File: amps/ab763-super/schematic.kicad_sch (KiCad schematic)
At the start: 112 parts, among them T1 125P5D · 360-0-360V, T2 125C1A, T3 125A9A, T4 125A20B

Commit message: Fix: deterministic schematic ids and wires split at every join
- _u() is uuid5 over (amp id, emission order), so a regeneration of an
  unchanged script is byte-identical and a drift gate becomes possible
- write() splits wire segments at symbol pins, wire ends and junction dots,
  so the file connects exactly what the drawing shows under KiCad's
  endpoint-only semantics (270 pins were on a wire's interior; net
  partitions unchanged on all 38 sheets)
- all sheets regenerated; aa864-bassman title block was stale (draft) and
  now matches meta.yaml (verified)

Co-Authored-By: Claude Fable 5.1 <noreply@anthropic.com>
Claude-Session: https://claude.ai/code/session_01KBMfdh37HmCL2iWcBiL5J1
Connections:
- net at RBIAS.1: now also DBIAS.2 (K)
- net at T3.1 (PRI_A): now also V7.1 (P)

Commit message: Fix: schematic wiring on ab763-twin, ab763, ab763-super
- long-tailed pair: the tail lead came off section B's PLATE pin; redrawn
  from its cathode on a joined-cathode lane under the bottle (all three)
- ab763-twin: V9/V10 plate run passed through V10's envelope and grounded
  cathode pin (one plate on ground, one floating); screen stubs 2 mm short
  of RSC1-4; V5B had no plate lead; driver grid bus through RGRD and CPIB
  riser through RFB1 (feedback node grounded); seven leads 4 mm short of
  their labels; VRBAL wiper carries -52 V per net_map
- ab763: same tail and RGRD faults; three pot ground flags 3.81 mm low;
  RNF2 had a wire ruled through its body
- ab763-super: V8 plate lead drawn from below its cathode; both reservoir
  bleeders shorted the supply to ground; RLV2 shorted by the stack output
  column; tremolo intensity feed ran through CTO1/VRSPD/RTO1 to ground;
  BP1 tap landed inside the choke body
- all three pass connectivity and verify_schematic_nets; no waivers

Co-Authored-By: Claude Fable 5.1 <noreply@anthropic.com>
Claude-Session: https://claude.ai/code/session_01KBMfdh37HmCL2iWcBiL5J1
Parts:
- removed C1: .1u 400V, symbol cx:C
- removed C11: 20u 525V, symbol cx:C
- removed CCR1: .003u, symbol cx:C
- removed CCV2: .02u, symbol cx:C
- removed CKTO1: 25u, symbol cx:C
- removed RBIAS: 470, symbol cx:R
- removed RKV2: 820, symbol cx:R
- removed RLR1: 100k, symbol cx:R
- removed RS2: 470 1W, symbol cx:R
- removed RTO2: 220k, symbol cx:R
- removed RTOG: 1M, symbol cx:R
- removed V6A: 12AT7, symbol cx:TRIODE
- removed V8: 6L6GC, symbol cx:PENTODE
- added C12: 20u 525V, symbol cx:C
- added C2: .1u 400V, symbol cx:C
- added CKV2: 25u, symbol cx:C
- added CPIB: .1u 200V, symbol cx:C
- added OPTO: neon + photocell, symbol cx:OPTO
- added RBL2: 220k 1W, symbol cx:R
- added RGR1: 220k, symbol cx:R
- added RST1: 1.5k, symbol cx:R
- added RTO1: 100k, symbol cx:R
- added V2B, V3A, V3B, V5: 12AX7, symbol cx:TRIODE
- C1: renamed from CPIB; value .1u 200V -> .1u 400V
- C11: renamed from RBL2; value 220k 1W -> 20u 525V; symbol cx:R -> cx:C
- CCD1: renamed from RKD1; value 820 -> .001u; symbol cx:R -> cx:C
- CCR1: renamed from RKR1; value 820 -> .003u; symbol cx:R -> cx:C
- CCV2: renamed from CKV2; value 25u -> .02u
- CKTO1: renamed from V5; value 12AX7 -> 25u; symbol cx:TRIODE -> cx:C
- CTO2: renamed from RTO1; value 100k -> .01u; symbol cx:R -> cx:C
- RBIAS: renamed from C12; value 20u 525V -> 470; symbol cx:C -> cx:R
- RKD1: renamed from V3A; value 12AX7 -> 820; symbol cx:TRIODE -> cx:R
- RKR1: renamed from V3B; value 12AX7 -> 820; symbol cx:TRIODE -> cx:R
- RKV2: renamed from RLV2; value 100k -> 820
- RLR1: renamed from RGR1; value 220k -> 100k
- RLV2: renamed from V2B; value 12AX7 -> 100k; symbol cx:TRIODE -> cx:R
- RS2: renamed from V7; value 6L6GC -> 470 1W; symbol cx:PENTODE -> cx:R
- RTO2: renamed from CCD1; value .001u -> 220k; symbol cx:C -> cx:R
- RTOG: renamed from CTO2; value .01u -> 1M; symbol cx:C -> cx:R
- V6A: renamed from OPTO; value neon + photocell -> 12AT7; symbol cx:OPTO -> cx:TRIODE
- V7: renamed from C2; value .1u 400V -> 6L6GC; symbol cx:C -> cx:PENTODE
- V8: renamed from RST1; value 1.5k -> 6L6GC; symbol cx:R -> cx:PENTODE
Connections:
- net BC: now also C12.1; no longer RBIAS.1
- net BD: now also RLR1.1; no longer CRS.2, RKV2.1, RKV2.2, RLV2.2 (G), SWBV.2, VRVV.2 (W)
- net BIAS TAP: now also DBIAS.1 (A)
- net BP1: now also C11.1, RD1.1, RS2.2, RTO2.1, T2.2
- net GND: now also RKD1.2, RKR1.2, RKV2.2, V7.4 (K), V8.4 (K), C12.2, CKV2.2, OPTO.2 (L2), OPTO.4 (P2), RBL2.2, RTO1.2, V5.2 (G); no longer C10.1, CCD1.2, CCR1.2, CCV2.2, CKTO1.1 (P), CTO1.1, CTO1.2, CTO2.2, RBIAS.2, RGRD.1, RINT.1, RS2.4 (K), T2.1, V4A.2 (G), V4B.2 (G), V6A.2 (L2), V6A.4 (P2), V9A.2 (K), V9B.2 (K), VRSPD.3
- net MIXG: now also CCV2.2, OPTO.3 (P1); no longer V6A.3 (P1)
- net NORM 1: now also R1n.1
- net NORM 2: now also R2n.1
- net PIG: now also CCD1.2, CPIA.1; no longer RTO2.2
- net RVSEND: now also RGRD.1, V4A.2 (G), V4B.2 (G)
- net SPKR: now also RNFB.1
- net TANK RET: now also RGR1.1
- net VIB 1: now also R1v.1
- net VIB 2: now also R2v.1
- net at DBIAS.2 (K): now also RBIAS.1
- net at CBIAS.1, VRBIAS.1: now also RBIAS.2, VRBIAS.2 (W)
- net at RKTO1.1: now also CKTO1.1, V5.3 (K); no longer CKTO1.3 (K)
- net at VRSPD.1: now also CTO1.2, CTO2.2, VRSPD.2 (W)
- net at RKR1.1: now also CKR1.1, V3B.3 (K)
- net at RLR1.2: now also CCR1.1, V3B.1 (P); no longer RKR1.2 (G)
- net at RGPB.2, V6B.2 (G): now also CPIB.2; no longer C1.2
- net at CPIA.2, RGPA.1: now also V6A.2 (G)
- net at C1.1: now also RLPA.2, V6A.1 (P); no longer RNFB.2
- net at RLPB.2, V6B.1 (P): now also C2.1; no longer RTAIL.2, V7.1
- net at VRREV.1: now also CCR1.2
- net at RS1.1: now also V7.3 (G2)
- net at CBD1.1, RGD1.1, RMR2.1: now also V3A.2 (G); no longer RKD1.2 (G)
- net at CCV2.1: now also CRS.2, RLV2.2, V2B.1 (P); no longer RLV2.3 (K)
- net at CBD1.2, RLD1.2: now also CCD1.1, V3A.1 (P); no longer RKD1.1 (P), RTO2.1
- net at RS2.1: now also V8.3 (G2); no longer T3.1 (PRI_A)
- net at T3.3 (PRI_B): now also V8.1 (P)
- net at RGL1.2: now also C1.2, RST1.1; no longer V8.1
- net at VRINT.1: now also CTO1.1, RTO2.2, VRINT.2 (W), V5.1 (P)
- net at VRINT.3: now also RINT.1
- net at RINT.2: now also OPTO.1 (L1); no longer V6A.1 (L1)
- net at RST2.2: now also V8.2 (G1)
- net at RGL2.1, RST2.1: now also C2.2; no longer V7.2
- net at RBL1.1: now also C10.1, T2.1, V9A.2 (K), V9B.2 (K), RBL2.1
- net at V6B.3 (K): now also RTAIL.2, V6A.3 (K)
- new net: CKD1.1, RKD1.1, V3A.3 (K)
- new net: RST1.2, V7.2 (G1)
- new net: RGR1.2, V3B.2 (G)
- new net: RTO1.1, VRSPD.3
- new net: SWBV.2, V2B.2 (G), VRVV.2 (W)
- new net: CKV2.1, RKV2.1, V2B.3 (K)
- new net: CPIB.1, RNFB.2
- new net: T3.1 (PRI_A), V7.1 (P)
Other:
- moved on the sheet: C1, CCV2, RGRD, RKV2, RLR1

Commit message: Fix: AB763 Super and 6G4 corrections read back from the factory sheets
AB763 Super (closes #15, closes #16)

The model omitted the Normal channel's second triode entirely and gave the
Vibrato second stage, mix driver and reverb recovery a cathode resistor each.
The C-FD schematic's boxed [A] and [E] are inter-stage connections: [A] ties
the Normal and Vibrato second stages to ONE 820 / 25u network, [E] ties the mix
driver and reverb recovery to another. Because our model omitted one triode's
current, this page claimed the printed chart was internally impossible at three
cathode nodes. It is not. With XV1B added and the shared nodes joined:

  KA   chart 2.1 V   was 1.5 V (-30.0%)   now 2.2 V (+3.6%)
  KE   chart 2.0 V   was 1.5 V (-27.0%)   now 2.2 V (+8.8%)
  PV2  chart 270 V   was 231 V (-14.4%)   now 277 V (+2.6%)

All 20 gated nodes now pass; the accusation is retracted in notes.md and the
retraction is recorded in meta.yaml as audit trail. This is the fourth time the
corpus has accused a factory sheet and been the one at fault.

The Middle control is 10 kOhm-A, not the 250 kOhm published -- 25x, so the
tone-stack curve was wrong, not just the label. Corrected everywhere including
the lab preset; the blackface mid-scoop returns at 15.6 dB / 419 Hz.

With the Middle pot confirmed, topology.tone_stack moves tb -> fmv: this
chassis carries a fixed bleed on one channel and a real Middle pot on the
other, and filing it as treble/bass contradicted its own parts list. The field
names the Vibrato channel and notes.md documents the mixed case.

6G4

Same presence idiom as the 6G5, read off the A-FJ sheet: a 1500 foot resistor
to ground with the 5K-L pot in series with a .1 cap paralleling it. The cap was
missing from the corpus; added as CPRES, 0.1uF, the 200 V read off the layout
page's own .1-200 lettering rather than defaulted from the notice's 400 V.

RNFB is 10 kOhm, not 56 -- traced end to end onto the OT secondary hot. RD1 is
4700 1W, not 10k: the netlist called t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
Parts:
- removed C1: .1u 400V, symbol cx:C
- removed CBV: .1u, symbol cx:C
- removed CCD1: .001u, symbol cx:C
- removed CKR1, CKV2: 25u, symbol cx:C
- removed CTO2: .01u, symbol cx:C
- removed R1v: 68k, symbol cx:R
- removed RBL1: 220k 1W, symbol cx:R
- removed RGPA, RGRD: 1M, symbol cx:R
- removed RGR1, RMR2: 220k, symbol cx:R
- removed RKD1, RKR1: 820, symbol cx:R
- removed RMR: 470k, symbol cx:R
- removed V2A: 12AX7, symbol cx:TRIODE
- removed VRVV: 1M-A vol, symbol cx:POT
- added C11: 20u 525V, symbol cx:C
- added CCN2: .047u, symbol cx:C
- added CCR1: .003u, symbol cx:C
- added CCV2: .02u, symbol cx:C
- added CKA, CKE: 25u, symbol cx:C
- added CRS: 500p, symbol cx:C
- added CTV: 250p, symbol cx:C
- added OPTO: neon + photocell, symbol cx:OPTO
- added RGL2: 220k 5%, symbol cx:R
- added RKE, RNFB: 820, symbol cx:R
- added RLN2, RLR1, RLV1: 100k, symbol cx:R
- added RTO2: 220k, symbol cx:R
- added RTOG: 1M, symbol cx:R
- added V1B: 12AX7, symbol cx:TRIODE
- C1: renamed from RGL2; value 220k 5% -> .1u 400V; symbol cx:R -> cx:C
- CBV: renamed from VRMV; value 250k-A mid -> .1u; symbol cx:POT -> cx:C
- CCD1: renamed from CTO1; value .01u -> .001u
- CTO1: renamed from RTOG; value 1M -> .01u; symbol cx:R -> cx:C
- CTO2: renamed from OPTO; value neon + photocell -> .01u; symbol cx:OPTO -> cx:C
- R1v: renamed from RLV1; value 100k -> 68k
- RBL1: renamed from C11; value 20u 525V -> 220k 1W; symbol cx:C -> cx:R
- RGPA: renamed from RNFB; value 820 -> 1M
- RGR1: renamed from CCR1; value .003u -> 220k; symbol cx:C -> cx:R
- RGRD: renamed from T4; value 125A20B -> 1M; symbol cx:OT_SE -> cx:R
- RKA: renamed from CRS; value 500p -> 820; symbol cx:C -> cx:R
- RMR: renamed from V3A; value 12AX7 -> 470k; symbol cx:TRIODE -> cx:R
- RMR2: renamed from CKD1; value 25u -> 220k; symbol cx:C -> cx:R
- SWBV: renamed from RKV2; value 820 -> Bright; symbol cx:R -> cx:SWITCH
- T4: renamed from RLR1; value 100k -> 125A20B; symbol cx:R -> cx:OT_SE
- V2A: renamed from CTV; value 250p -> 12AX7; symbol cx:C -> cx:TRIODE
- V2B: renamed from CCV2; value .02u -> 12AX7; symbol cx:C -> cx:TRIODE
- V3A: renamed from RTO2; value 220k -> 12AX7; symbol cx:R -> cx:TRIODE
- VRMV: renamed from SWBV; value Bright -> 10k-A mid; symbol cx:SWITCH -> cx:POT
- VRVV: renamed from V2B; value 12AX7 -> 1M-A vol; symbol cx:TRIODE -> cx:POT
- renumbered V1 to V1A
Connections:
- net -52V: now also RGL2.2; no longer C1.2
- net BD: now also RLN2.1, RLR1.1, RLV1.1; no longer R1v.1, T4.1
- net BP1: now also C11.1, RTO2.1; no longer RBL1.1, V3A.1
- net GND: now also CTO2.1, RGRD.2, RKA.2, T4.4 (SEC_C), VRMV.3, VRVV.3, C11.2, CKA.2, CKE.2, OPTO.2 (L2), OPTO.4 (P2), RKE.2, RTOG.1, RTOG.2; no longer CBV.3, CTO1.1, CTO1.2, CTO2.2 (L2), CTO2.4 (P2), RGRD.4 (SEC_C), SWBV.2
- net MIXG: now also RMR.2, CCV2.2, OPTO.3 (P1); no longer CTO2.3 (P1), V2B.2
- net PIG: now also CCD1.2
- net REVERB TANK: now also T4.3 (SEC_H); no longer RGRD.3 (SEC_H)
- net RVSEND: now also RGRD.1, CRS.1; no longer RKA.1
- net SPKR: now also RNFB.1; no longer RGPA.1
- net TANK RET: now also RGR1.1
- net VIB 1: now also R1v.1
- net at CBV2.1, RSV.2: now also CBV.1
- net at RINT.2: now also OPTO.1 (L1); no longer CTO2.1 (L1)
- net at RGR1.2: now also V3B.2 (G); no longer VRREV.1
- net at CBD1.2, RLD1.2: now also CCD1.1, V3A.1 (P); no longer RMR.1 (P)
- net at CBD1.1, RGD1.1: now also RMR2.1, V3A.2 (G); no longer RMR.2 (G)
- net at RGPB.1, RT2.1, RTAIL.1: now also RGPA.2
- net at RGL1.2, RST1.1: now also C1.2
- net at VRREV.2 (W): now also RMR.1
- net at RSV.1, V2A.1 (P): now also CTV.1, RLV1.2; no longer R1v.2
- net at VRSPD.1, VRSPD.2 (W): now also CTO1.2, CTO2.2; no longer CCD1.2
- net KE: now reaches V3B.3 (K)
- net KE: now also V3A.3 (K), CKE.1, RKE.1
- net at V5.1 (P), VRINT.1, VRINT.2 (W): now also CTO1.1, RTO2.2; no longer CCD1.1, V3A.2
- net at C2.2, RST2.1: now also RGL2.1; no longer C1.1
- net at RLPA.2, V6A.1 (P): now also C1.1
- net at SWBN.2, VRVN.2 (W): now also V1B.2 (G); no longer RMD1.1
- net at CKV1.1, RKV1.1: now also V2A.3 (K)
- net at C10.1, RBL2.1, T2.1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: now also RBL1.1
- net at V2A.2 (G): now also R1v.2, R2v.2, RGV1.1; no longer VRTV.1
- net at CBRV.1, VRTV.2 (W): now also VRVV.1
- net at CPIA.2, V6A.2 (G): now also RGPA.1
- net at RLV2.2, V2B.1 (P): now also CCV2.1, CRS.2; no longer RKA.2, VRVV.1 (P)
- net at VRMV.1: now also VRBV.3, VRMV.2 (W); no longer CBRV.2
- net at VRVV.2 (W): now also SWBV.2, V2B.2 (G); no longer VRMV.2
- net at SWBV.1: now also CBRV.2; no longer VRVV.3 (K)
- net at CPIB.1: now also RNFB.2; no longer RGPA.2
- new net: CTV.2, VRTV.1
- new net: CCN2.2, RMD1.1
- new net: CCN2.1, RLN2.2, V1B.1 (P)
- new net: CCR1.1, RLR1.2, V3B.1 (P)
- new net: CCR1.2, VRREV.1
- new net KA: CKA.1, RKA.1, V1B.3 (K), V2B.3 (K)
- now unconnected: CBV.2 (W), T4.2
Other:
- note added: "1"
- note added: "2"
- note added: "3"
- note added: "4"
- note added: "5"
- note added: "6"
- note added: "7"
- note added: "8"
- moved on the sheet: CCD1, R1v, RGPA, VRMV

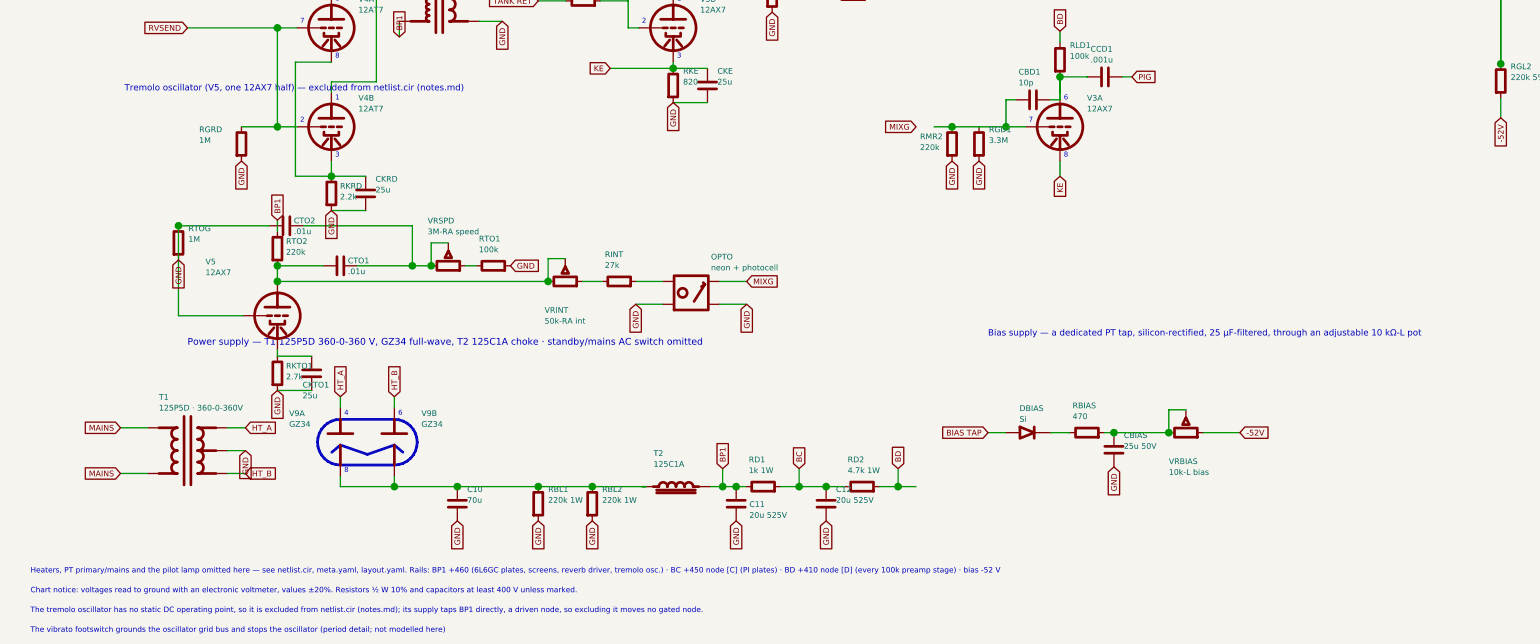
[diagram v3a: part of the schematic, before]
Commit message: Fix: schematic sheet notes no longer name repository files
Thirty-seven committed sheets rendered footnotes and section notes such as
"Heaters and PT primary omitted — see netlist.cir and meta.yaml" or
"excluded from netlist.cir (notes.md)" to visitors through KiCanvas. The
prose sweeps never counted sheets. Rewritten in the site's own words — the
netlist, the sources list, the circuit story, the parts list, the board
drawing — in 59 strings across 33 draw scripts, keeping every technical
claim as it was; the three tone sheets (6G4, 6G5, 6G6-B) are under repair
elsewhere and keep theirs for now. The sweep touched only strings passed to
the sheet's note, text, caption and footnote calls, never a path or a value.

Gates: check_schematics 40/0, connectivity 0 isolated pins;
verify_schematic_nets 40 clean; only the regenerated sheets and their served
copies changed.

Co-Authored-By: Claude Fable 5.1 <noreply@anthropic.com>
Claude-Session: https://claude.ai/code/session_01KBMfdh37HmCL2iWcBiL5J1
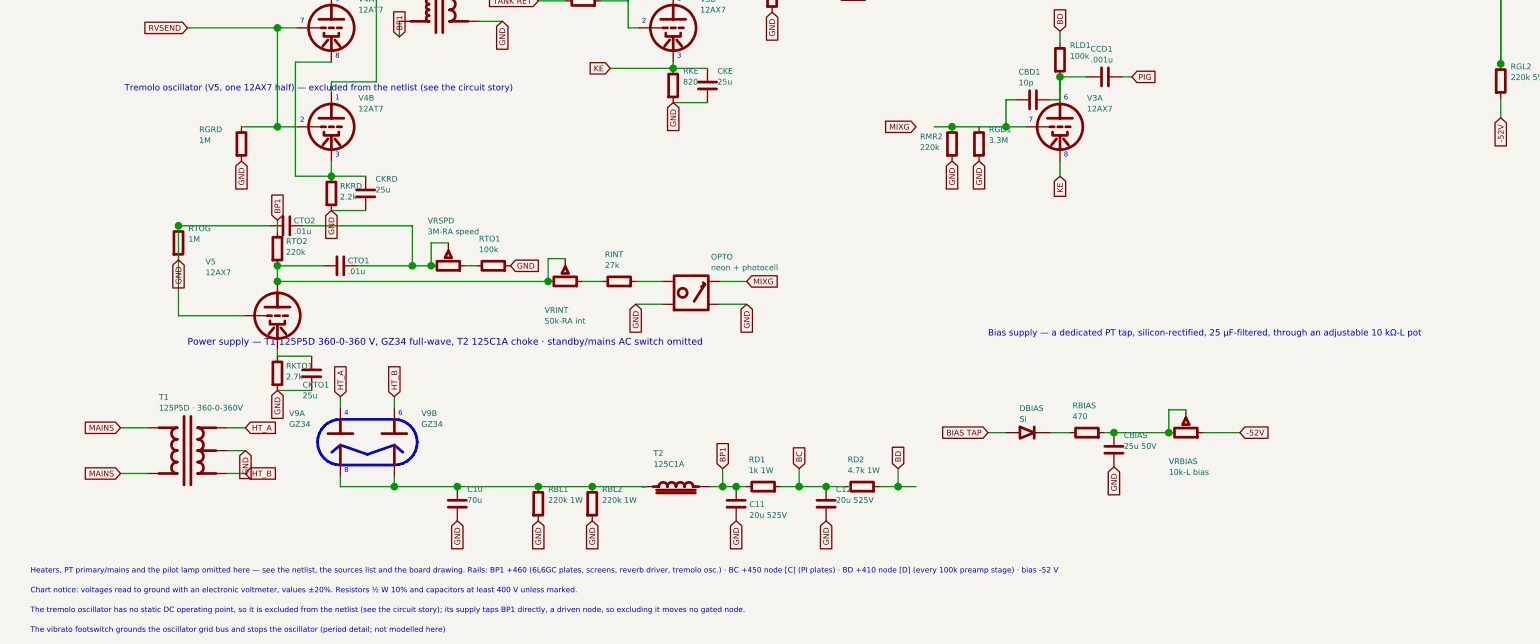
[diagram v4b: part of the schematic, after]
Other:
- note added: "Heaters, PT primary/mains and the pilot lamp omitted here — see the netlist, the sources list and the board drawing. Rails: BP1 +460 (6L6GC plates, screens, reverb driver, tremolo osc.) · BC +450 node [C] (PI plates) · BD +410 node [D] (every 100k preamp stage) · bias -52 V"
- note added: "The tremolo oscillator has no static DC operating point, so it is excluded from the netlist (see the circuit story); its supply taps BP1 directly, a driven node, so excluding it moves no gated node."
- note added: "Tremolo oscillator (V5, one 12AX7 half) — excluded from the netlist (see the circuit story)"
- note removed: "Heaters, PT primary/mains and the pilot lamp omitted here — see netlist.cir, meta.yaml, layout.yaml. Rails: BP1 +460 (6L6GC plates, screens, reverb driver, tremolo osc.) · BC +450 node [C] (PI plates) · BD +410 node [D] (every 100k preamp stage) · bias -52 V"
- note removed: "The tremolo oscillator has no static DC operating point, so it is excluded from netlist.cir (notes.md); its supply taps BP1 directly, a driven node, so excluding it moves no gated node."
- note removed: "Tremolo oscillator (V5, one 12AX7 half) — excluded from netlist.cir (notes.md)"
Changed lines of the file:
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@@
   (global_label "PIG" (shape input) (at 257.609 154.789 0)
     (effects (font (size 1.27 1.27)) (justify left)))
-  (text "Tremolo oscillator (V5, one 12AX7 half) — excluded from netlist.cir (notes.md)" (at 33.6088 157.389 0)
+  (text "Tremolo oscillator (V5, one 12AX7 half) — excluded from the netlist (see the circuit story)" (at 33.6088 157.389 0)
     (effects (font (size 1.4 1.4)) (justify left)))
   (symbol (lib_id "cx:TRIODE") (at 67.6088 207.889 0) (unit 1)
@@
   (text "6" (at 94.4588 229.659 0)
     (effects (font (size 1.1 1.1)) (justify left)))
-  (text "Heaters, PT primary/mains and the pilot lamp omitted here — see netlist.cir, meta.yaml, layout.yaml. Rails: BP1 +460 (6L6GC plates, screens, reverb driver, tremolo osc.) · BC +450 node [C] (PI plates) · BD +410 node [D] (every 100k preamp stage) · bias -52 V" (at 12.7 264.667 0)
+  (text "Heaters, PT primary/mains and the pilot lamp omitted here — see the netlist, the sources list and the board drawing. Rails: BP1 +460 (6L6GC plates, screens, reverb driver, tremolo osc.) · BC +450 node [C] (PI plates) · BD +410 node [D] (every 100k preamp stage) · bias -52 V" (at 12.7 264.667 0)
     (effects (font (size 1.2 1.2)) (justify left)))
   (text "Chart notice: voltages read to ground with an electronic voltmeter, values ±20%. Resistors ½ W 10% and capacitors at least 400 V unless marked." (at 12.7 269.067 0)
     (effects (font (size 1.2 1.2)) (justify left)))
-  (text "The tremolo oscillator has no static DC operating point, so it is excluded from netlist.cir (notes.md); its supply taps BP1 directly, a driven node, so excluding it moves no gated node." (at 12.7 273.467 0)
+  (text "The tremolo oscillator has no static DC operating point, so it is excluded from the netlist (see the circuit story); its supply taps BP1 directly, a driven node, so excluding it moves no gated node." (at 12.7 273.467 0)
     (effects (font (size 1.2 1.2)) (justify left)))
   (text "The vibrato footswitch grounds the oscillator grid bus and stops the oscillator (period detail; not modelled here)" (at 12.7 277.867 0)
